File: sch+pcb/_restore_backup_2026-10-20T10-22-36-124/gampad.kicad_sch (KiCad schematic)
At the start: 26 parts, among them J1 swd header, J10 Conn_01x01, J3 Conn_01x01, J4 Conn_01x01, J5 Conn_01x01, J6 Conn_01x01, J7 Conn_01x01, J8 Conn_01x01, J9 Conn_01x01, U1 STM32L442KCUx, U2 MIC5504-3.3YM5

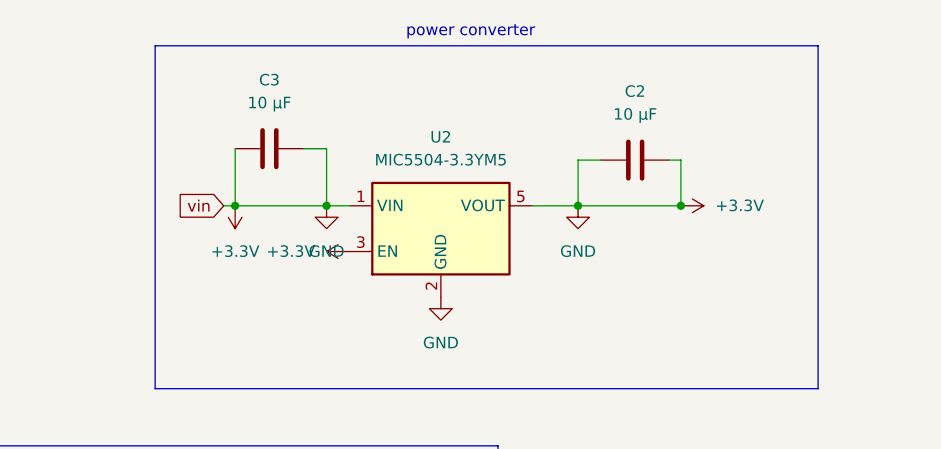
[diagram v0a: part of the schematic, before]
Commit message: updated readme and gbr files to the new stuff
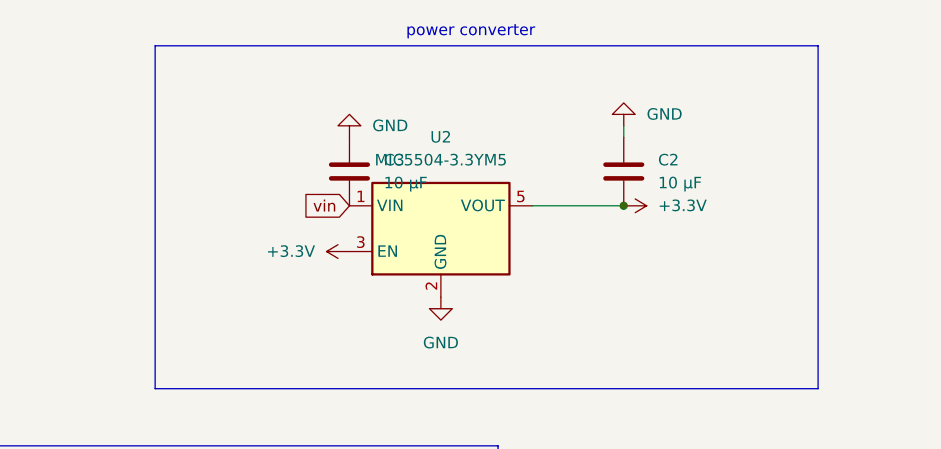
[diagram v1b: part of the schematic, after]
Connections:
- net +3.3V: no longer C1.2, C2.2, C3.1, C3.2, C4.2, C5.1, D1.1 (K), D2.1 (K), J1.3 (Pin_3), J2.A1 (GND), J2.A12 (GND), J2.A4 (VBUS), J2.A9 (VBUS), J2.B1 (GND), J2.B12 (GND), J2.B4 (VBUS), J2.B9 (VBUS), R3.2, R4.2, U1.16 (VSS), U1.32 (VSS), U1.33 (VSS), U2.1 (VIN), U2.2 (GND)
- new net GND: C1.2, C2.2, C3.2, C4.2, C5.1, D1.1 (K), D2.1 (K), J1.3 (Pin_3), J2.A1 (GND), J2.A12 (GND), J2.B1 (GND), J2.B12 (GND), R3.2, R4.2, U1.16 (VSS), U1.32 (VSS), U1.33 (VSS), U2.2 (GND)
- new net vin: C3.1, J2.A4 (VBUS), J2.A9 (VBUS), J2.B4 (VBUS), J2.B9 (VBUS), U2.1 (VIN)
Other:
- moved on the sheet: C2, C3
